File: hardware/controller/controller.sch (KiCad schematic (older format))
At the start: 49 parts, among them IC1 ATMEGA164A-P, IC2 MAX3232, IC3 MAX485, J1 DB9, K1 CONN_3_V, P1 CONN_02X03, P3 CONN_01X02, P4 CONN_01X04, SW1 SW_RESET, SW2 SW_PUSH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

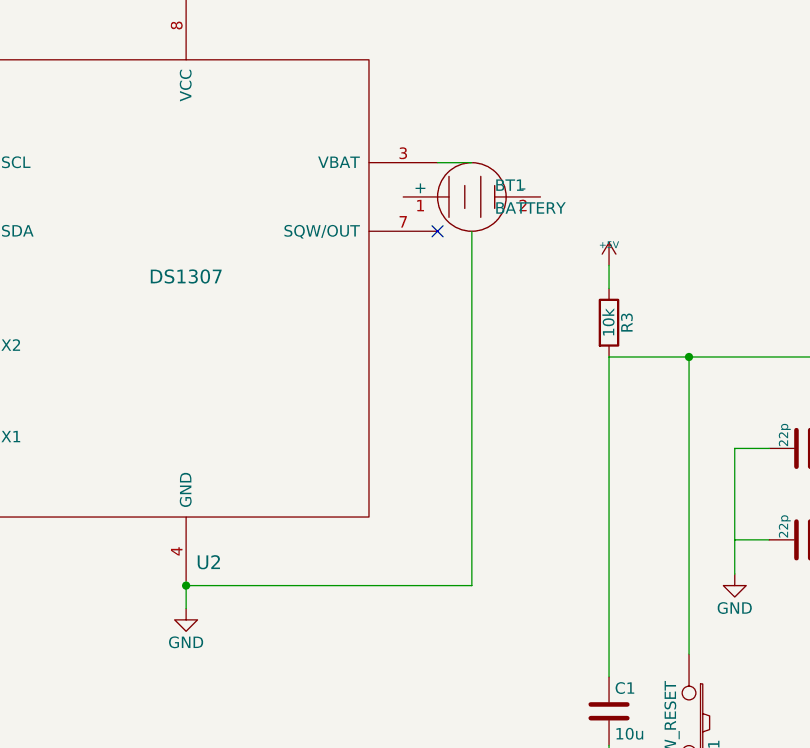
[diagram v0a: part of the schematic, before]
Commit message: Improved digital input circuit
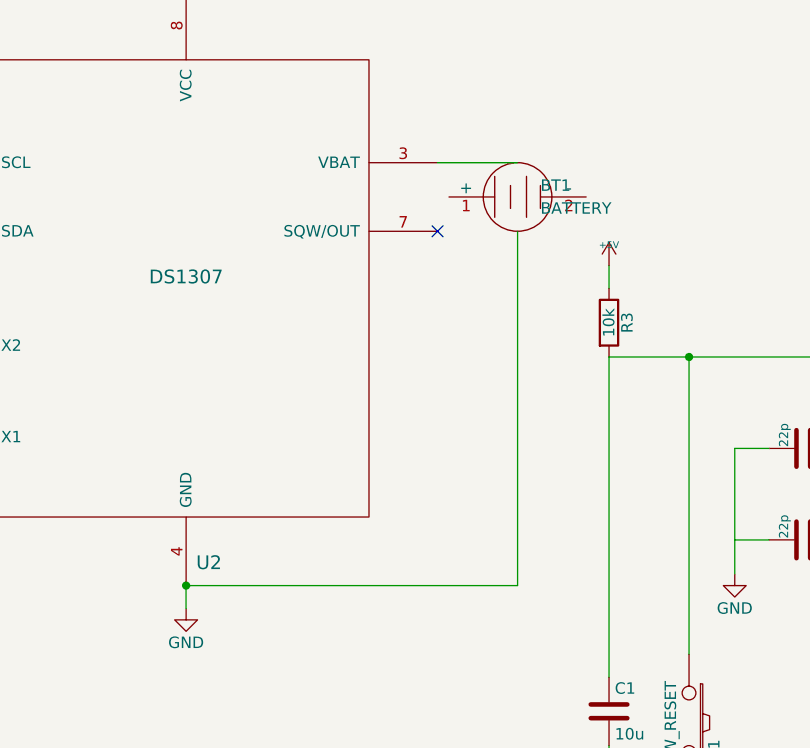
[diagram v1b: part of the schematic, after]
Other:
- moved on the sheet: BT1
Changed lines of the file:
@@
 LIBS:contrib
 LIBS:valves
+LIBS:ADCchain
+LIBS:BP5037
+LIBS:DS1882
+LIBS:dual_mos_p
+LIBS:hirose
+LIBS:lm1117
+LIBS:LT1054
+LIBS:lumex
+LIBS:MAX4582
+LIBS:MCP23017
+LIBS:MCP42010
+LIBS:myconn3
+LIBS:PJ-102A
+LIBS:xmossupport
 LIBS:relays
 LIBS:interface
+LIBS:ok-74logic
+LIBS:ok-con-generic
+LIBS:ok-diodes
+LIBS:ok-generic
+LIBS:ok-ic-analog
+LIBS:ok-ic-atmel
+LIBS:ok-ic-com
+LIBS:ok-ic-memory
+LIBS:ok-ic-power
+LIBS:ok-ic-special
+LIBS:ok-ic-stm32
+LIBS:ok-jacks
+LIBS:ok-opto
+LIBS:ok-power
+LIBS:ok-relay
+LIBS:ok-switches
+LIBS:ok-transformers
+LIBS:ok-transistors
 LIBS:ds1307timer-cache
 LIBS:borniers
@@
 Sheet 1 1
 Title "Hovedkort"
-Date "4 jun 2015"
+Date "5 jun 2015"
 Rev "1"
 Comp "Haustveit elektro"
@@
 L BATTERY BT1
 U 1 1 556DD9B7
-P 5500 3350
-F 0 "BT1" H 5600 3400 50  0000 L CNN
-F 1 "BATTERY" H 5600 3300 50  0000 L CNN
-F 2 "" V 5500 3390 60  0000 C CNN
-F 3 "" V 5500 3390 60  0000 C CNN
-	1    5500 3350
+P 5700 3350
+F 0 "BT1" H 5800 3400 50  0000 L CNN
+F 1 "BATTERY" H 5800 3300 50  0000 L CNN
+F 2 "" V 5700 3390 60  0000 C CNN
+F 3 "" V 5700 3390 60  0000 C CNN
+	1    5700 3350
 	1    0    0    -1
 $EndComp
@@
 	2700 4400 3100 4400
 Wire Wire Line
-	5500 3200 5350 3200
-Wire Wire Line
-	5500 3500 5500 5050
-Wire Wire Line
-	5500 5050 4250 5050
+	5700 3200 5350 3200
+Wire Wire Line
+	5700 3500 5700 5050
+Wire Wire Line
+	5700 5050 4250 5050
 Wire Wire Line
 	14350 4150 9500 4150
